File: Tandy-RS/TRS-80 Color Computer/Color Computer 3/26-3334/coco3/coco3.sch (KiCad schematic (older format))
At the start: 7 parts, among them CN1 Conn_02x20_Odd_Even

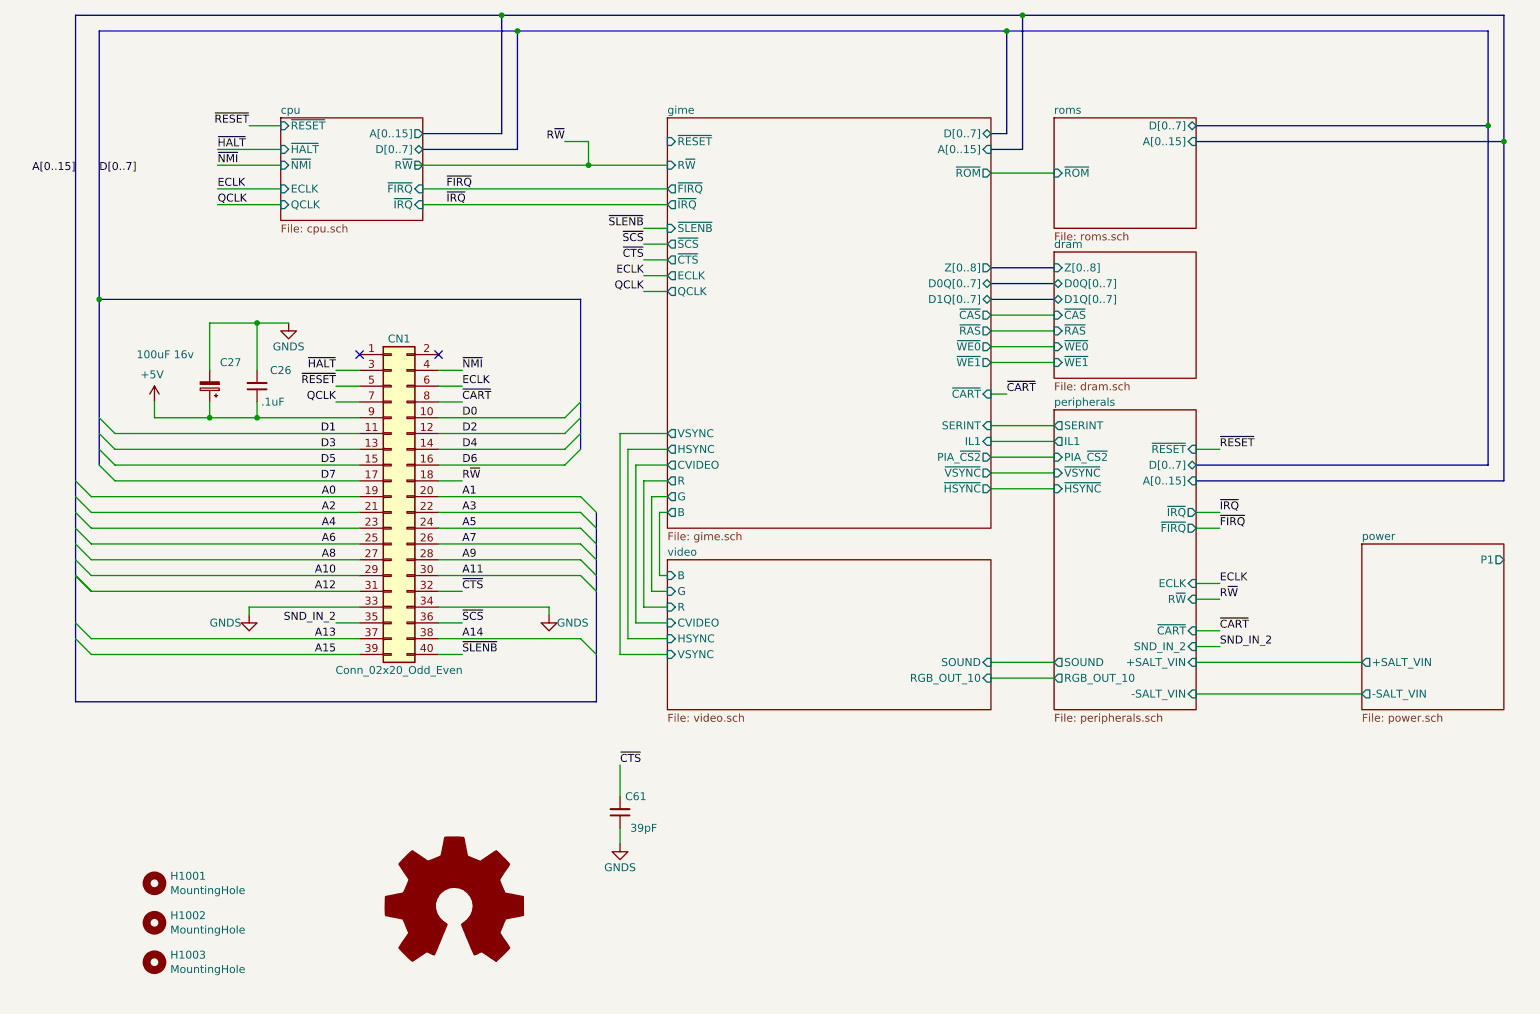
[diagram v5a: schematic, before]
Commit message: finished video sheet
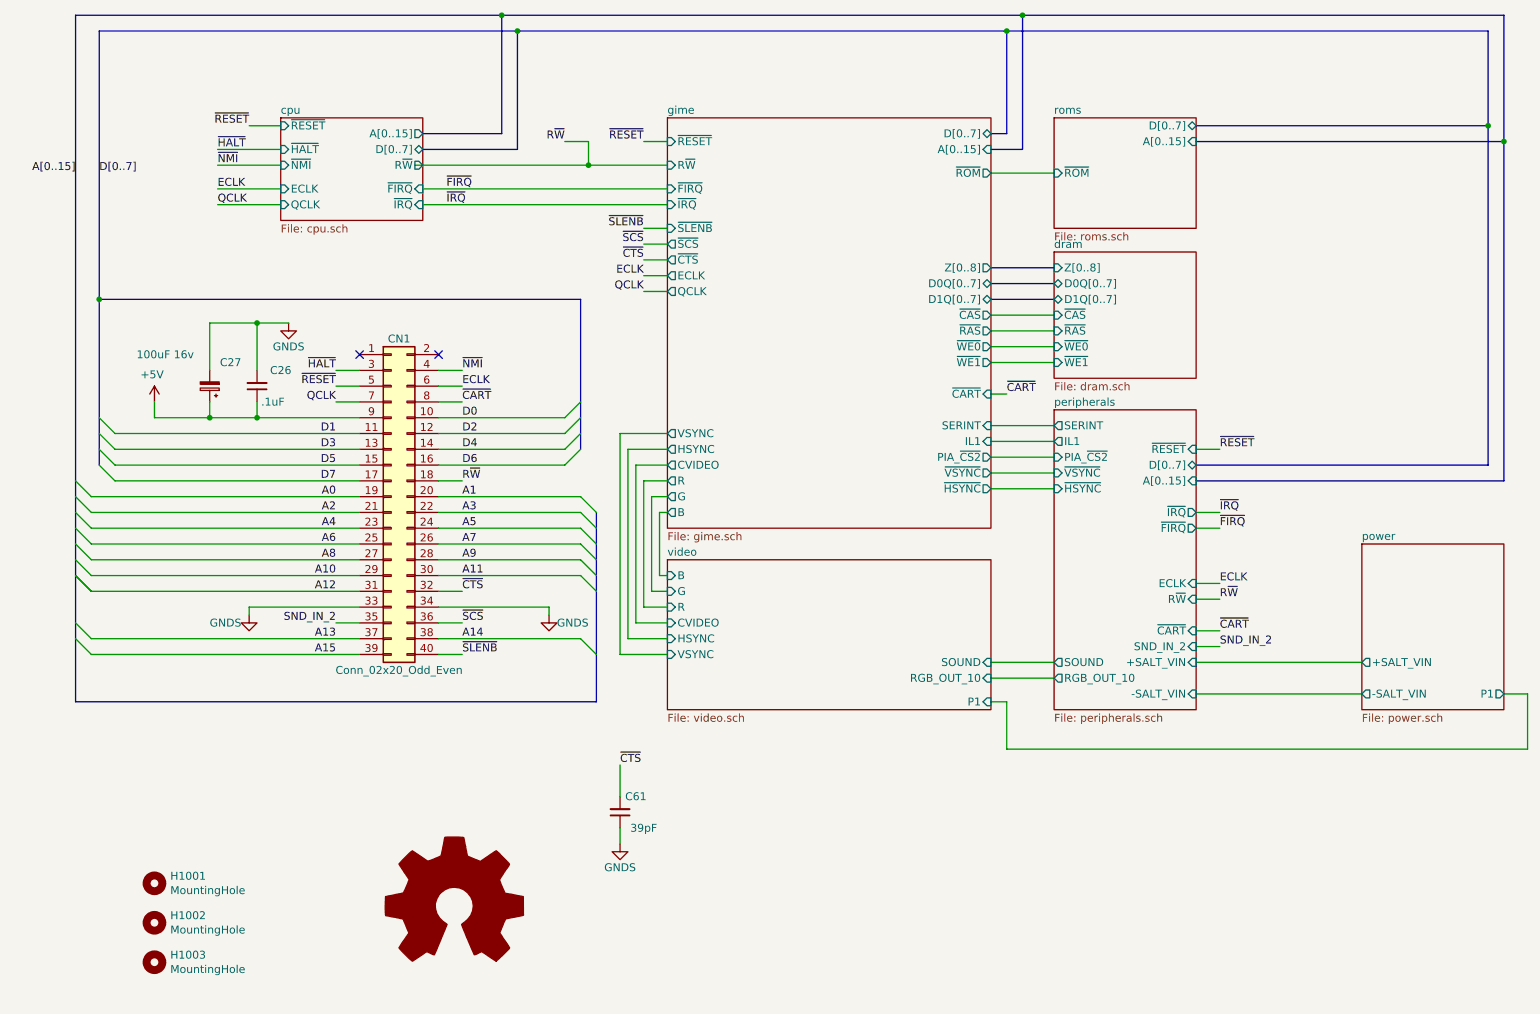
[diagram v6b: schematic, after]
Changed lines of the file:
@@
 F2 "-SALT_VIN" O L 9000 5750 50
 F3 "+SALT_VIN" O L 9000 5550 50
-F4 "P1" O R 9900 4900 50
+F4 "P1" O R 9900 5750 50
 $EndSheet
 Wire Bus Line
@@
 F8 "VSYNC" I L 4600 5500 50
 F9 "SOUND" I R 6650 5550 50
+F10 "P1" I R 6650 5800 50
 $EndSheet
 Wire Wire Line
@@
 F0 "gime" 50
 F1 "gime.sch" 50
-F2 "~IRQ" O L 4600 2650 50
-F3 "~FIRQ" O L 4600 2550 50
-F4 "~RESET" I L 4600 2250 50
-F5 "R~W" I L 4600 2400 50
-F6 "D0Q[0..7]" B R 6650 3150 50
-F7 "D1Q[0..7]" B R 6650 3250 50
-F8 "Z[0..8]" O R 6650 3050 50
-F9 "D[0..7]" B R 6650 2200 50
-F10 "A[0..15]" I R 6650 2300 50
-F11 "R" O L 4600 4400 50
-F12 "G" O L 4600 4500 50
-F13 "B" O L 4600 4600 50
-F14 "CVIDEO" O L 4600 4300 50
-F15 "SERINT" I R 6650 4050 50
-F16 "IL1" I R 6650 4150 50
-F17 "~CART" I R 6650 3850 50
-F18 "~SLENB" I L 4600 2800 50
-F19 "~SCS" O L 4600 2900 50
-F20 "~CTS" O L 4600 3000 50
-F21 "~ROM" O R 6650 2450 50
-F22 "PIA_~CS2" O R 6650 4250 50
-F23 "ECLK" O L 4600 3100 50
-F24 "QCLK" O L 4600 3200 50
-F25 "VSYNC" O L 4600 4100 50
-F26 "HSYNC" O L 4600 4200 50
-F27 "~WE0" O R 6650 3550 50
-F28 "~WE1" O R 6650 3650 50
-F29 "~CAS" O R 6650 3350 50
-F30 "~RAS" O R 6650 3450 50
-F31 "~VSYNC" O R 6650 4350 50
-F32 "~HSYNC" O R 6650 4450 50
+F2 "~RESET" I L 4600 2250 50
+F3 "R~W" I L 4600 2400 50
+F4 "D0Q[0..7]" B R 6650 3150 50
+F5 "D1Q[0..7]" B R 6650 3250 50
+F6 "Z[0..8]" O R 6650 3050 50
+F7 "D[0..7]" B R 6650 2200 50
+F8 "A[0..15]" I R 6650 2300 50
+F9 "R" O L 4600 4400 50
+F10 "G" O L 4600 4500 50
+F11 "B" O L 4600 4600 50
+F12 "CVIDEO" O L 4600 4300 50
+F13 "SERINT" I R 6650 4050 50
+F14 "IL1" I R 6650 4150 50
+F15 "~CART" I R 6650 3850 50
+F16 "~SLENB" I L 4600 2800 50
+F17 "~SCS" O L 4600 2900 50
+F18 "~CTS" O L 4600 3000 50
+F19 "~ROM" O R 6650 2450 50
+F20 "PIA_~CS2" O R 6650 4250 50
+F21 "ECLK" O L 4600 3100 50
+F22 "QCLK" O L 4600 3200 50
+F23 "VSYNC" O L 4600 4100 50
+F24 "HSYNC" O L 4600 4200 50
+F25 "~WE0" O R 6650 3550 50
+F26 "~WE1" O R 6650 3650 50
+F27 "~CAS" O R 6650 3350 50
+F28 "~RAS" O R 6650 3450 50
+F29 "~VSYNC" O R 6650 4350 50
+F30 "~HSYNC" O R 6650 4450 50
+F31 "~IRQ" I L 4600 2650 50
+F32 "~FIRQ" I L 4600 2550 50
 $EndSheet
 NoConn ~ 2650 3600
@@
 Wire Wire Line
 	7050 5550 6650 5550
+Wire Wire Line
+	9900 5750 10050 5750
+Wire Wire Line
+	10050 5750 10050 6100
+Wire Wire Line
+	10050 6100 6750 6100
+Wire Wire Line
+	6750 6100 6750 5800
+Wire Wire Line
+	6750 5800 6650 5800
+Text Label 4450 2250 2    50   ~ 0
+~RESET
+Wire Wire Line
+	4600 2250 4450 2250
 Wire Bus Line
 	1000 3250 1000 4300

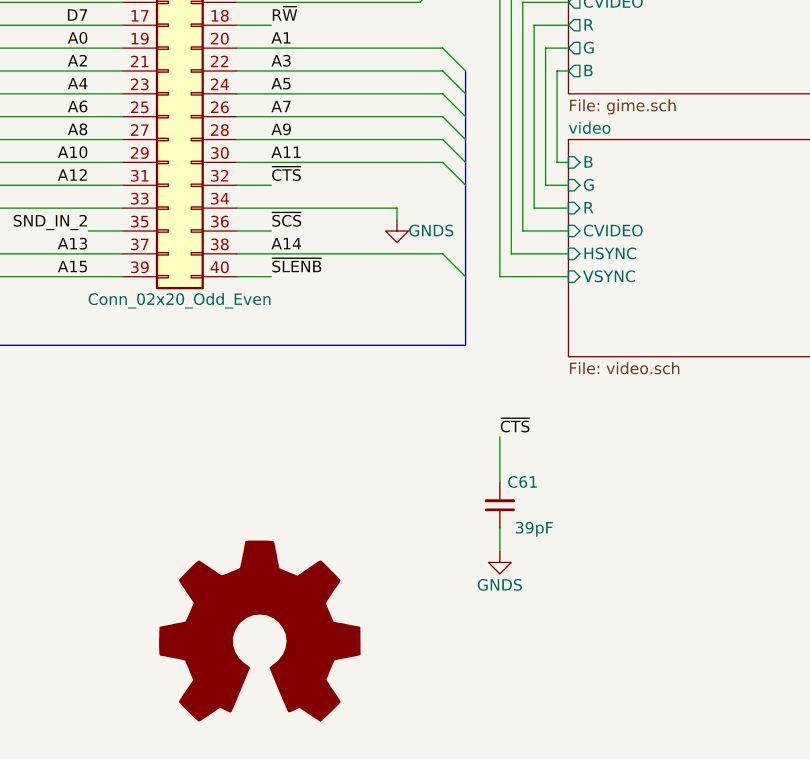
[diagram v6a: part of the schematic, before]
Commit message: found and added lost capacitor c68
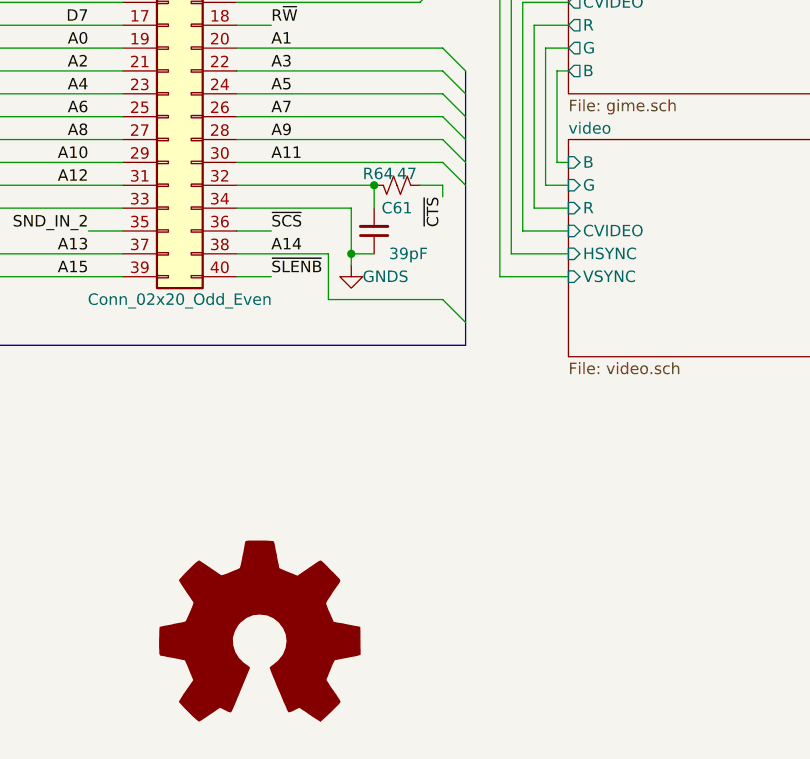
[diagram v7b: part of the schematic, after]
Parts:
- added R64: 47, Resistor_THT:R_Axial_DIN0309_L9.0mm_D3.2mm_P12.70mm_Horizontal, symbol Device:R_Small_US
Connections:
- net ~CTS: now also R64.1; no longer C61.2, CN1.32 (Pin_32)
- new net: C61.2, CN1.32 (Pin_32), R64.2
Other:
- moved on the sheet: C61
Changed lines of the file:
@@
 	1    0    0    -1
 $EndComp
-Wire Wire Line
-	3150 5200 3850 5200
-Wire Wire Line
-	3850 5250 3850 5200
 $Comp
 L power:GNDS #PWR?
 U 1 1 60A24DD1
-P 3850 5250
+P 3650 5450
 AR Path="/602A51A8/60A24DD1" Ref="#PWR?"  Part="1"
 AR Path="/60308A73/60A24DD1" Ref="#PWR?"  Part="1"
@@
 AR Path="/603D345E/60A24DD1" Ref="#PWR?"  Part="1"
 AR Path="/60A24DD1" Ref="#PWR01005"  Part="1"
-F 0 "#PWR01005" H 3850 5000 50  0001 C CNN
-F 1 "GNDS" H 3700 5200 50  0000 C CNN
-F 2 "" H 3850 5250 50  0001 C CNN
-F 3 "" H 3850 5250 50  0001 C CNN
-	1    3850 5250
+F 0 "#PWR01005" H 3650 5200 50  0001 C CNN
+F 1 "GNDS" H 3500 5400 50  0000 C CNN
+F 2 "" H 3650 5450 50  0001 C CNN
+F 3 "" H 3650 5450 50  0001 C CNN
+	1    3650 5450
 	-1   0    0    -1
 $EndComp
@@
 $EndComp
 Wire Wire Line
-	4050 5400 3150 5400
-Wire Wire Line
 	3150 5000 4050 5000
 Wire Wire Line
@@
 	4050 4700 3150 4700
 Entry Wire Line
-	4050 5400 4150 5500
+	4050 5600 4150 5700
 Entry Wire Line
 	4050 5000 4150 5100
@@
 Text Label 3300 5000 0    50   ~ 0
 A11
-Wire Wire Line
-	3150 5100 3300 5100
-Text Label 3300 5100 0    50   ~ 0
+Text Label 4050 5150 3    50   ~ 0
 ~CTS
 Wire Wire Line
@@
 L Device:C_Small C?
 U 1 1 613A25D3
-P 4300 6500
+P 3750 5300
 AR Path="/60273794/613A25D3" Ref="C?"  Part="1"
 AR Path="/602A51A8/613A25D3" Ref="C?"  Part="1"
@@
 AR Path="/61257512/613A25D3" Ref="C?"  Part="1"
 AR Path="/613A25D3" Ref="C61"  Part="1"
-F 0 "C61" H 4400 6400 50  0000 C CNN
-F 1 "39pF" H 4450 6600 50  0000 C CNN
-F 2 "Capacitor_THT:C_Disc_D4.7mm_W2.5mm_P5.00mm" H 4300 6500 50  0001 C CNN
-F 3 " https://www.vishay.com/docs/45171/kseries.pdf" H 4300 6500 50  0001 C CNN
-F 4 "digikey" V 4300 6500 50  0001 C CNN "Vendor"
-F 5 "BC1008CT-ND" V 4300 6500 50  0001 C CNN "Vendor part#"
-F 6 "K390J15C0GF5TL2" V 4300 6500 50  0001 C CNN "Manufacturer part#"
-	1    4300 6500
+F 0 "C61" H 3850 5200 50  0000 C CNN
+F 1 "39pF" H 3900 5400 50  0000 C CNN
+F 2 "Capacitor_THT:C_Disc_D4.7mm_W2.5mm_P5.00mm" H 3750 5300 50  0001 C CNN
+F 3 " https://www.vishay.com/docs/45171/kseries.pdf" H 3750 5300 50  0001 C CNN
+F 4 "digikey" V 3750 5300 50  0001 C CNN "Vendor"
+F 5 "BC1008CT-ND" V 3750 5300 50  0001 C CNN "Vendor part#"
+F 6 "K390J15C0GF5TL2" V 3750 5300 50  0001 C CNN "Manufacturer part#"
+	1    3750 5300
 	1    0    0    1
 $EndComp
-$Comp
-L power:GNDS #PWR?
-U 1 1 613BBC94
-P 4300 6700
-AR Path="/602A51A8/613BBC94" Ref="#PWR?"  Part="1"
-AR Path="/60308A73/613BBC94" Ref="#PWR?"  Part="1"
-AR Path="/603E4732/613BBC94" Ref="#PWR?"  Part="1"
-AR Path="/603D345E/613BBC94" Ref="#PWR?"  Part="1"
-AR Path="/613BBC94" Ref="#PWR01002"  Part="1"
-F 0 "#PWR01002" H 4300 6450 50  0001 C CNN
-F 1 "GNDS" H 4300 6550 50  0000 C CNN
-F 2 "" H 4300 6700 50  0001 C CNN
-F 3 "" H 4300 6700 50  0001 C CNN
-	1    4300 6700
-	1    0    0    -1
-$EndComp
-Text Label 4300 6200 0    50   ~ 0
-~CTS
-Wire Wire Line
-	4300 6200 4300 6400
-Wire Wire Line
-	4300 6600 4300 6700
 Text Label 2500 5300 2    50   ~ 0
 SND_IN_2
@@
 Wire Wire Line
 	4600 2250 4450 2250
+Wire Wire Line
+	3550 5400 3550 5600
+Wire Wire Line
+	3550 5600 4050 5600
+Wire Wire Line
+	3150 5400 3550 5400
+Wire Wire Line
+	3150 5200 3650 5200
+Wire Wire Line
+	3650 5200 3650 5400
+Wire Wire Line
+	3150 5100 3750 5100
+Wire Wire Line
+	3750 5100 3750 5200
+Wire Wire Line
+	3750 5400 3650 5400
+Connection ~ 3650 5400
+Wire Wire Line
+	3650 5400 3650 5450
+$Comp
+L Device:R_Small_US R?
+U 1 1 614AF842
+P 3850 5100
+AR Path="/60273794/614AF842" Ref="R?"  Part="1"
+AR Path="/61257512/614AF842" Ref="R?"  Part="1"
+AR Path="/614AF842" Ref="R64"  Part="1"
+F 0 "R64" V 3900 4950 50  0000 L CNN
+F 1 "47" V 3900 5100 50  0000 L CNN
+F 2 "Resistor_THT:R_Axial_DIN0309_L9.0mm_D3.2mm_P12.70mm_Horizontal" H 3850 5100 50  0001 C CNN
+F 3 "https://www.seielect.com/catalog/sei-cf_cfm.pdf" H 3850 5100 50  0001 C CNN
+F 4 "digikey" H 3850 5100 50  0001 C CNN "Vendor"
+F 5 "CF12JT47R0CT-ND" H 3850 5100 50  0001 C CNN "Vendor part#"
+F 6 "CF12JT47R0" H 3850 5100 50  0001 C CNN "Manufacturer part#"
+	1    3850 5100
+	0    1    -1   0
+$EndComp
+Connection ~ 3750 5100
+Wire Wire Line
+	3950 5100 4050 5100
+Wire Wire Line
+	4050 5100 4050 5150
 Wire Bus Line
 	1000 3250 1000 4300

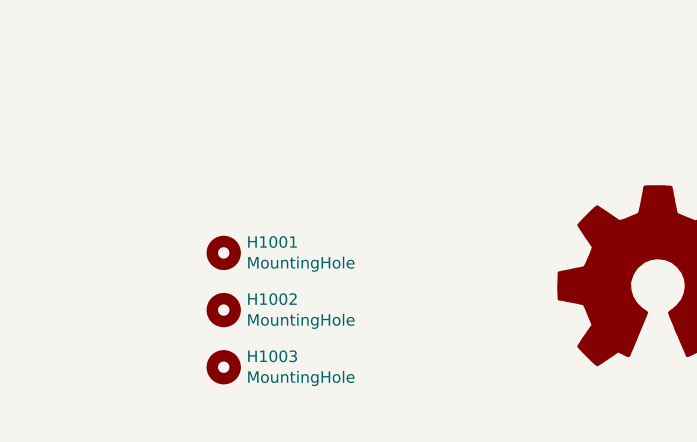
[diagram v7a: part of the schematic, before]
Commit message: -swapped 5v to 8v inthe video section. -swapped collector and emitter connections for Q1 -sourced more coponents -started pcb
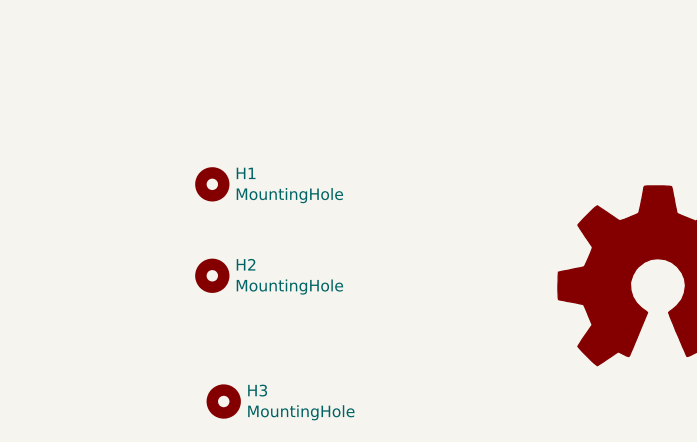
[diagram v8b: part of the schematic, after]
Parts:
- removed H1001: MountingHole, MountingHole:MountingHole_4.5mm, symbol Mechanical:MountingHole
- removed H1002, H1003: MountingHole, MountingHole:MountingHole_4mm, symbol Mechanical:MountingHole
- added H1, H2: MountingHole, MountingHole:MountingHole_3.5mm, symbol Mechanical:MountingHole
- added H3: MountingHole, coco2:coco3_outline_and_layout, symbol Mechanical:MountingHole
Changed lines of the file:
@@
 	2150 2150 1950 2150
-$Comp
-L Mechanical:MountingHole H1001
-U 1 1 60AD1126
-P 1350 6950
-F 0 "H1001" H 1450 6996 50  0000 L CNN
-F 1 "MountingHole" H 1450 6905 50  0000 L CNN
-F 2 "MountingHole:MountingHole_4.5mm" H 1350 6950 50  0001 C CNN
-F 3 "~" H 1350 6950 50  0001 C CNN
-	1    1350 6950
-	1    0    0    -1
-$EndComp
-$Comp
-L Mechanical:MountingHole H1002
-U 1 1 60AD16B9
-P 1350 7200
-F 0 "H1002" H 1450 7246 50  0000 L CNN
-F 1 "MountingHole" H 1450 7155 50  0000 L CNN
-F 2 "MountingHole:MountingHole_4mm" H 1350 7200 50  0001 C CNN
-F 3 "~" H 1350 7200 50  0001 C CNN
-	1    1350 7200
-	1    0    0    -1
-$EndComp
-$Comp
-L Mechanical:MountingHole H1003
-U 1 1 60AD74E1
-P 1350 7450
-F 0 "H1003" H 1450 7496 50  0000 L CNN
-F 1 "MountingHole" H 1450 7405 50  0000 L CNN
-F 2 "MountingHole:MountingHole_4mm" H 1350 7450 50  0001 C CNN
-F 3 "~" H 1350 7450 50  0001 C CNN
-	1    1350 7450
-	1    0    0    -1
-$EndComp
 $Comp
 L Graphic:Logo_Open_Hardware_Large #LOGO1001
@@
 Wire Wire Line
 	4050 5100 4050 5150
+$Comp
+L Mechanical:MountingHole H1
+U 1 1 61042AD1
+P 1300 6650
+F 0 "H1" H 1400 6696 50  0000 L CNN
+F 1 "MountingHole" H 1400 6605 50  0000 L CNN
+F 2 "MountingHole:MountingHole_3.5mm" H 1300 6650 50  0001 C CNN
+F 3 "~" H 1300 6650 50  0001 C CNN
+	1    1300 6650
+	1    0    0    -1
+$EndComp
+$Comp
+L Mechanical:MountingHole H2
+U 1 1 61042DE1
+P 1300 7050
+F 0 "H2" H 1400 7096 50  0000 L CNN
+F 1 "MountingHole" H 1400 7005 50  0000 L CNN
+F 2 "MountingHole:MountingHole_3.5mm" H 1300 7050 50  0001 C CNN
+F 3 "~" H 1300 7050 50  0001 C CNN
+	1    1300 7050
+	1    0    0    -1
+$EndComp
+$Comp
+L Mechanical:MountingHole H3
+U 1 1 6103A7A8
+P 1350 7600
+F 0 "H3" H 1450 7646 50  0000 L CNN
+F 1 "MountingHole" H 1450 7555 50  0000 L CNN
+F 2 "coco2:coco3_outline_and_layout" H 1350 7600 50  0001 C CNN
+F 3 "~" H 1350 7600 50  0001 C CNN
+	1    1350 7600
+	1    0    0    -1
+$EndComp
 Wire Bus Line
 	1000 3250 1000 4300
